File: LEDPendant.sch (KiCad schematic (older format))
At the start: 14 parts

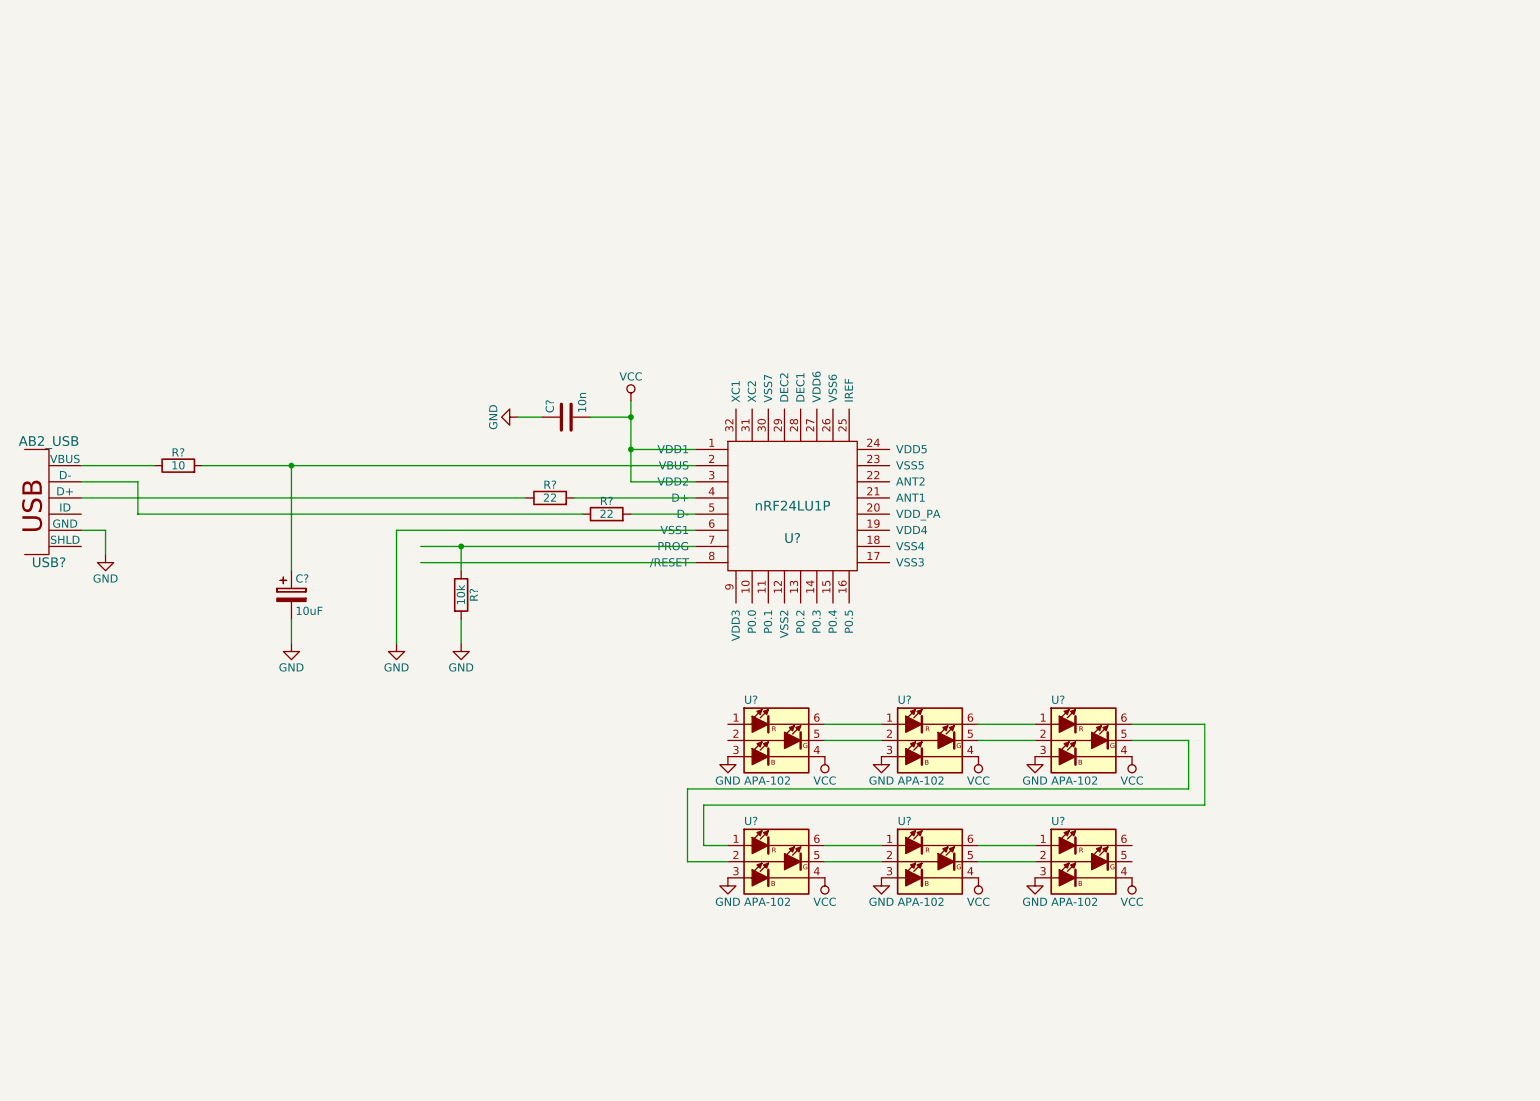
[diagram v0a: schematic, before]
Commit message: Added antenna and more wires
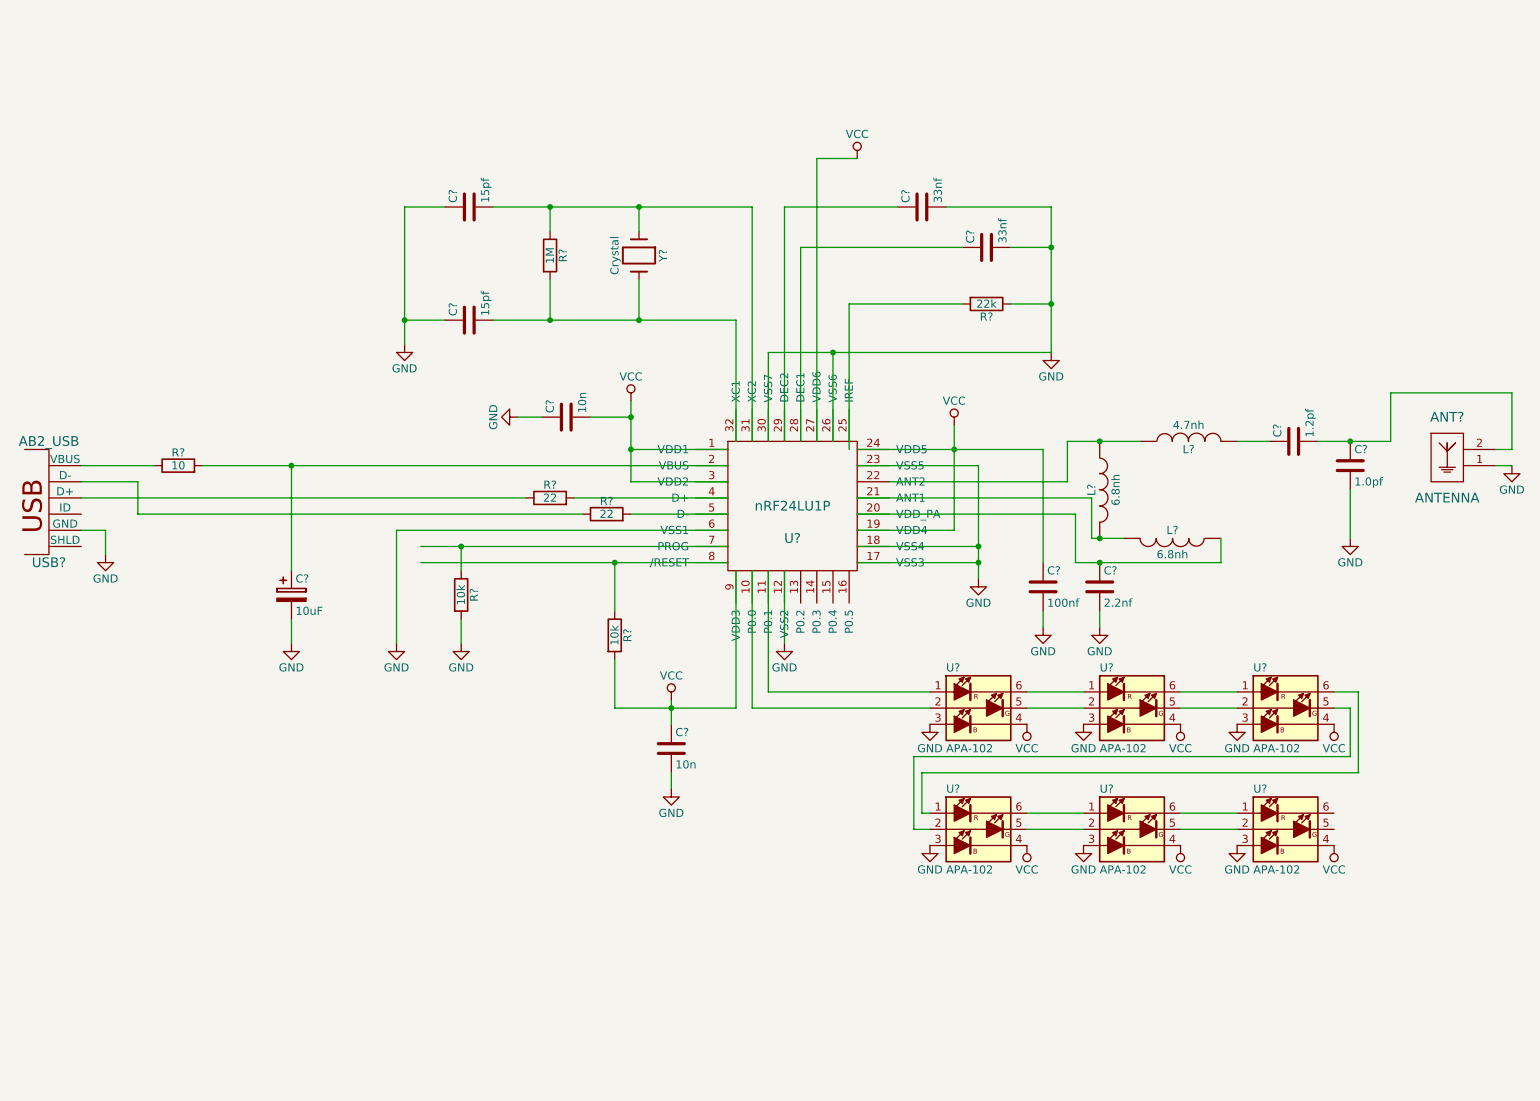
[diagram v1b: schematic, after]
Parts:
- added ANT?: ANTENNA, symbol ANTENNA
- added C?: 10n, symbol C
- added C? (x2): 15pf, symbol C
- added C? (x2): 33nf, symbol C
- added C?: 100nf, symbol C
- added C?: 2.2nf, symbol C
- added C?: 1.2pf, symbol C
- added C?: 1.0pf, symbol C
- added L? (x2): 6.8nh, symbol INDUCTOR
- added L?: 4.7nh, symbol INDUCTOR
- added R?: 10k, symbol R
- added R?: 1M, symbol R
- added R?: 22k, symbol R
- added Y?: Crystal, symbol Crystal
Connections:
- wire segments 45 -> 106
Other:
- moved on the sheet: U?

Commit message: Placed and somewhat autorouted
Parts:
- added C12: 10uF, Capacitors_Tantalum_SMD:TantalC_SizeA_EIA-3216_Reflow, symbol CP
- added C13: 0.1uF, Capacitors_SMD:C_0805, symbol C
- added U8: LD1117S33TR, SMD_Packages:SOT-223, symbol LD1117S33TR
- ANT1: renamed from ANT?; footprint (none) -> antennes:Ant_Microchip_2_4G
- C1: renamed from C?; footprint (none) -> Capacitors_Tantalum_SMD:TantalC_SizeA_EIA-3216_Reflow
- C10, C11, C2, C3, C4, C5, C6, C7, C8, C9: renamed from C?; footprint (none) -> Capacitors_SMD:C_0805
- L1, L2, L3: renamed from L?; footprint (none) -> Resistors_SMD:R_0805
- R1, R2, R3, R4, R5, R6, R7: renamed from R?; footprint (none) -> Resistors_SMD:R_0805
- U1: renamed from U?; footprint (none) -> Housings_DFN_QFN:QFN-32-1EP_5x5mm_Pitch0.5mm
- U2, U3, U4, U5, U6, U7: renamed from U?; footprint (none) -> CrumpPrints:APA102
- USB1: renamed from USB?; footprint (none) -> ab2_usb:AB2_USB_MICRO_SMD
- Y1: renamed from Y?; footprint (none) -> Crystals:Crystal_SMD_0603_4Pads
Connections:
- net labels added: +BATT
- wire segments 106 -> 115
- no-connect marks 0 -> 8
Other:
- moved on the sheet: ANT1

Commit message: Another pass at the large board
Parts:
- added R10: 22k, symbol R
- added R11: 47k, symbol R
- added R8: 100k, symbol R
- added R9: 10k, symbol R
- added SW1, SW2, SW3: SPST, symbol SPST
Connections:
- net GND: now also R8.1
- net VCC: now also R10.1, R11.1, R9.1
- net at U1.13 (P0.2): now also R8.2, SW1.1, SW2.1, SW3.1
- new net: R9.2, SW1.2
- new net: R10.2, SW2.2
- new net: R11.2, SW3.2
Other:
- moved on the sheet: U2, U3, U4, U5, U6, U7

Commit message: More hand routing
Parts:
- R10, R11, R8, R9: footprint (none) -> Resistors_SMD:R_0805
- SW1, SW2, SW3: footprint (none) -> Buttons_Switches_SMD:SW_SPST_PTS645
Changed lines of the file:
@@
 F 0 "R9" V 6980 5250 50  0000 C CNN
 F 1 "10k" V 6900 5250 50  0000 C CNN
-F 2 "" V 6830 5250 30  0000 C CNN
+F 2 "Resistors_SMD:R_0805" V 6830 5250 30  0001 C CNN
 F 3 "" H 6900 5250 30  0000 C CNN
 	1    6900 5250
@@
 F 0 "R10" V 7180 5250 50  0000 C CNN
 F 1 "22k" V 7100 5250 50  0000 C CNN
-F 2 "" V 7030 5250 30  0000 C CNN
+F 2 "Resistors_SMD:R_0805" V 7030 5250 30  0001 C CNN
 F 3 "" H 7100 5250 30  0000 C CNN
 	1    7100 5250
@@
 F 0 "R11" V 7380 5250 50  0000 C CNN
 F 1 "47k" V 7300 5250 50  0000 C CNN
-F 2 "" V 7230 5250 30  0000 C CNN
+F 2 "Resistors_SMD:R_0805" V 7230 5250 30  0001 C CNN
 F 3 "" H 7300 5250 30  0000 C CNN
 	1    7300 5250
@@
 F 0 "R8" V 6080 5150 50  0000 C CNN
 F 1 "100k" V 6000 5150 50  0000 C CNN
-F 2 "" V 5930 5150 30  0000 C CNN
+F 2 "Resistors_SMD:R_0805" V 5930 5150 30  0001 C CNN
 F 3 "" H 6000 5150 30  0000 C CNN
 	1    6000 5150
@@
 F 0 "SW1" H 6400 5700 50  0000 C CNN
 F 1 "SPST" H 6400 5500 50  0000 C CNN
-F 2 "" H 6400 5600 60  0000 C CNN
+F 2 "Buttons_Switches_SMD:SW_SPST_PTS645" H 6400 5600 60  0001 C CNN
 F 3 "" H 6400 5600 60  0000 C CNN
 	1    6400 5600
@@
 F 0 "SW2" H 6600 5950 50  0000 C CNN
 F 1 "SPST" H 6600 5750 50  0000 C CNN
-F 2 "" H 6600 5850 60  0000 C CNN
+F 2 "Buttons_Switches_SMD:SW_SPST_PTS645" H 6600 5850 60  0001 C CNN
 F 3 "" H 6600 5850 60  0000 C CNN
 	1    6600 5850
@@
 F 0 "SW3" H 6800 6200 50  0000 C CNN
 F 1 "SPST" H 6800 6000 50  0000 C CNN
-F 2 "" H 6800 6100 60  0000 C CNN
+F 2 "Buttons_Switches_SMD:SW_SPST_PTS645" H 6800 6100 60  0001 C CNN
 F 3 "" H 6800 6100 60  0000 C CNN
 	1    6800 6100
